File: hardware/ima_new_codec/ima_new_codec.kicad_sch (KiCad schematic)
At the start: 5 parts, among them J1 DM3AT-SF-PEJM5, U1 STM32F722RETx, Y3 Crystal_GND24

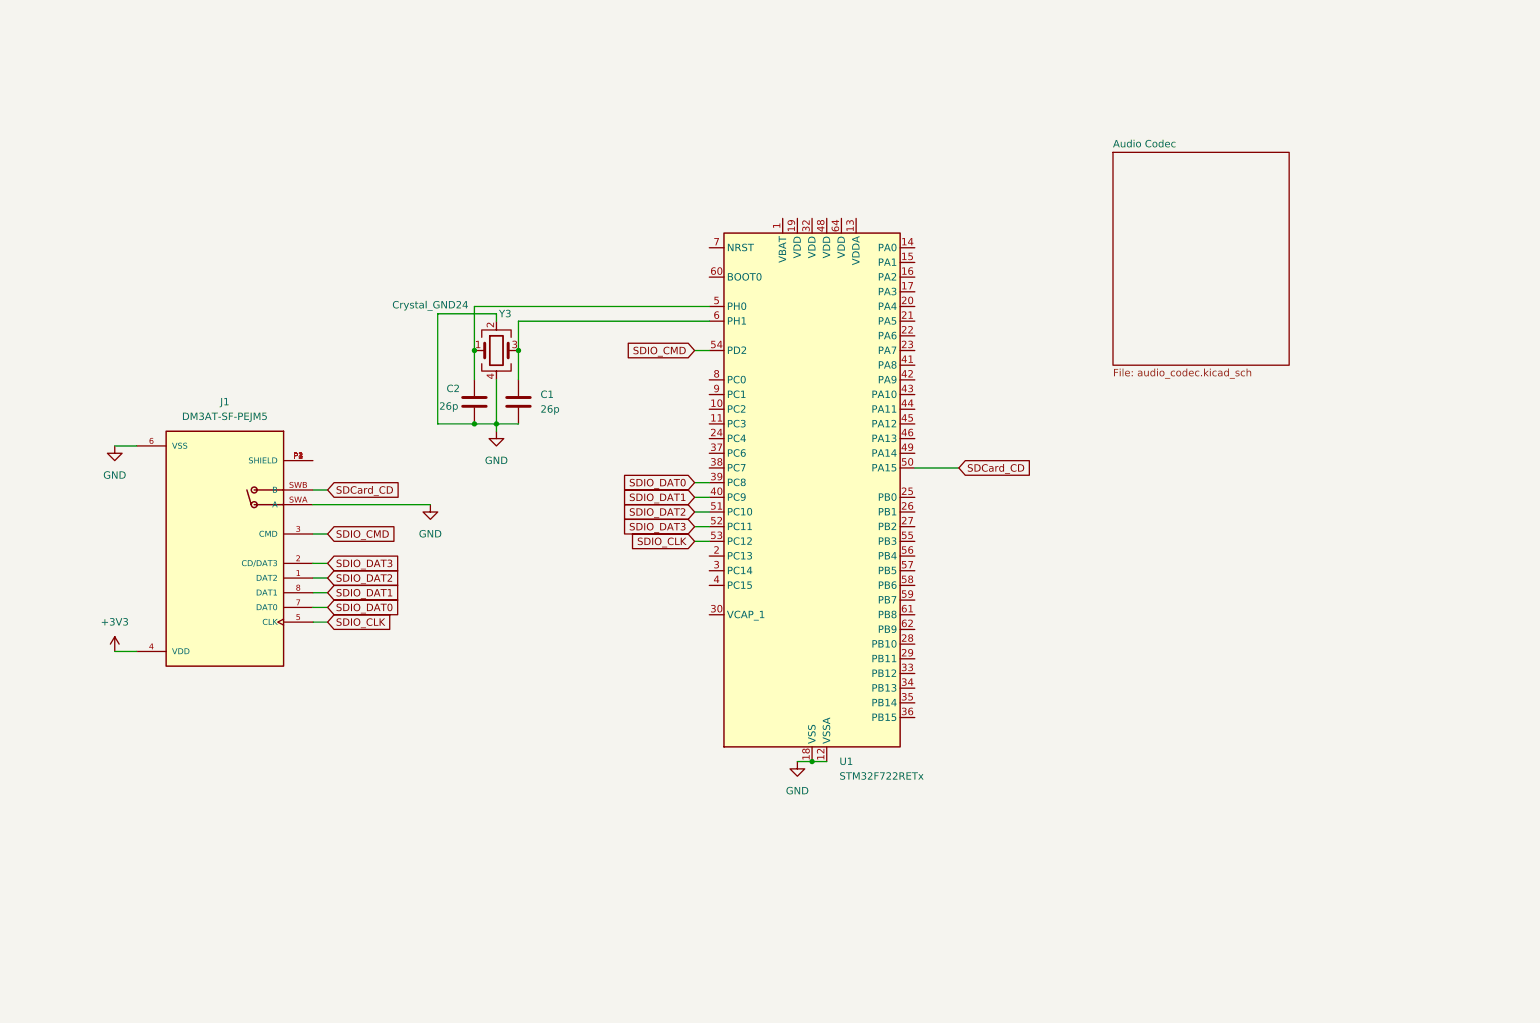
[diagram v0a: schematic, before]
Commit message: migrate to stm32h7 mcu
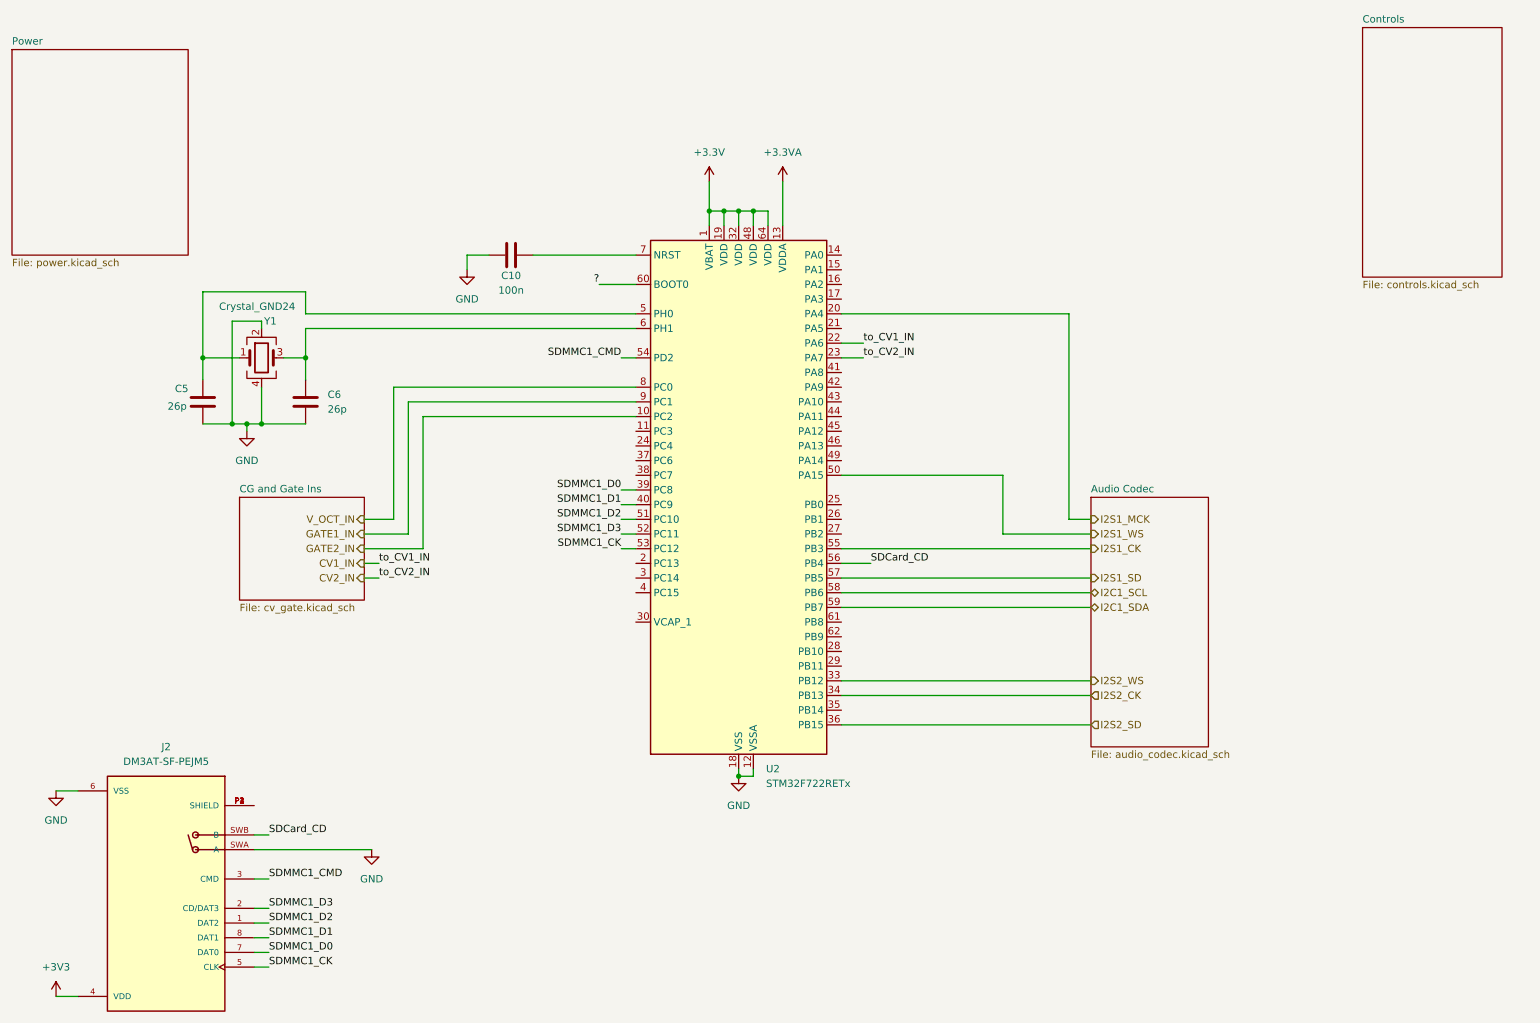
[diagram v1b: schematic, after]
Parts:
- added C10: 100n, symbol Device:C
- renumbered C2 to C5, C1 to C6, J1 to J2, U1 to U2, Y3 to Y1
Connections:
- net GND: now also C10.1
- net SDCard_CD: now also U2.56 (PB4); no longer U2.50 (PA15)
- net +3.3V: now reaches U2.1 (VBAT)
- net +3.3V: now also U2.19 (VDD), U2.32 (VDD), U2.48 (VDD), U2.64 (VDD)
- net GATE2_IN: now reaches U2.10 (PC2)
- net +3.3VA: now reaches U2.13 (VDDA)
- net I2S1_MCK: now reaches U2.20 (PA4)
- net CV1_IN: now reaches U2.22 (PA6)
- net CV2_IN: now reaches U2.23 (PA7)
- net I2S2_WS: now reaches U2.33 (PB12)
- net I2S2_CK: now reaches U2.34 (PB13)
- net I2S2_SD: now reaches U2.36 (PB15)
- net I2S1_CK: now reaches U2.55 (PB3)
- net I2S1_SD: now reaches U2.57 (PB5)
- net I2C1_SCL: now reaches U2.58 (PB6)
- net I2C1_SDA: now reaches U2.59 (PB7)
- net ?: now reaches U2.60 (BOOT0)
- net at U2.7 (NRST): now also C10.2
- net V_OCT_IN: now reaches U2.8 (PC0)
- net GATE1_IN: now reaches U2.9 (PC1)
- net SDIO_CLK renamed SDMMC1_CK
- net SDIO_CMD renamed SDMMC1_CMD
- net SDIO_DAT0 renamed SDMMC1_D0
- net SDIO_DAT1 renamed SDMMC1_D1
- net SDIO_DAT2 renamed SDMMC1_D2
- net SDIO_DAT3 renamed SDMMC1_D3
- new net I2S1_WS: U2.50 (PA15)
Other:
- added sheet CG and Gate Ins (cv_gate.kicad_sch)
- added sheet Controls (controls.kicad_sch)
- added sheet Power (power.kicad_sch)
- moved on the sheet: C5, C6, J2, U2, Y1
